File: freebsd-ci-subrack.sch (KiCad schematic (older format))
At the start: 63 parts

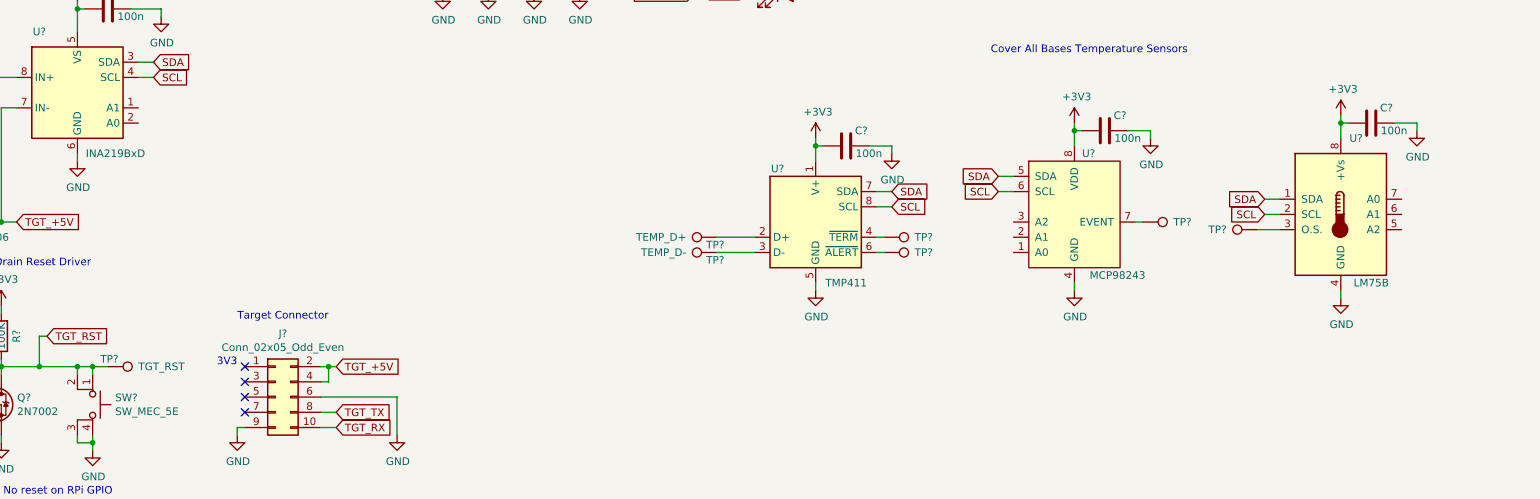
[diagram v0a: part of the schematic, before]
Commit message: I2C address assignment
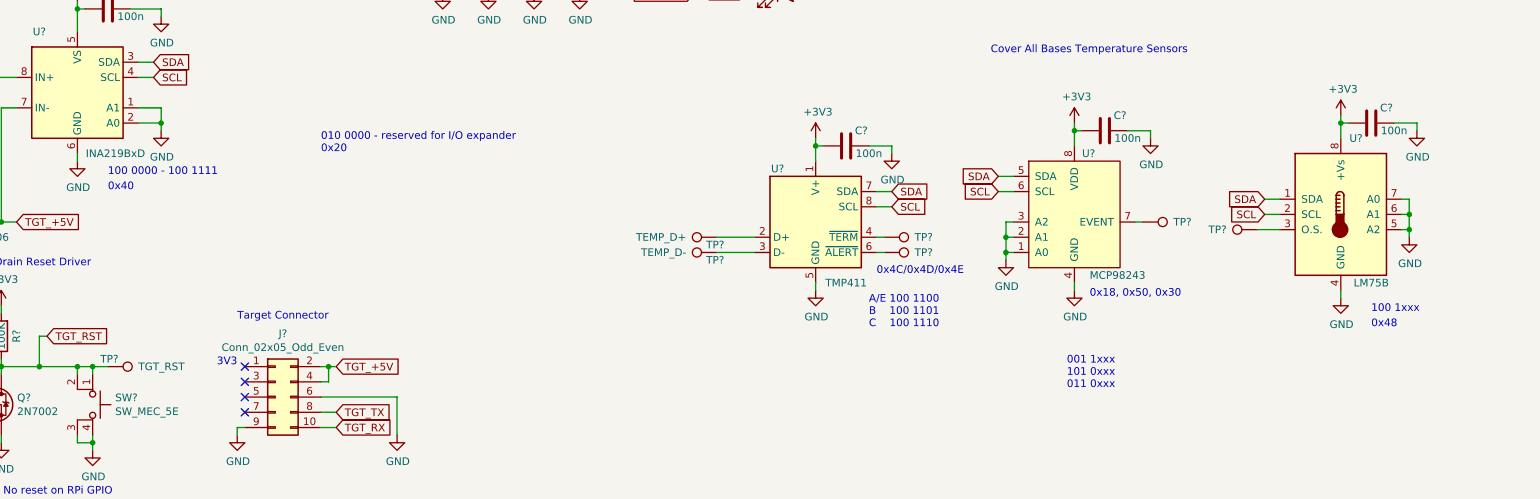
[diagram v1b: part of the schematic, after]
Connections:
- net GND: now also U?.1 (A0), U?.1 (A1), U?.2 (A0), U?.2 (A1), U?.3 (A2), U?.5 (A2), U?.6 (A1), U?.7 (A0)
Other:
- note added: "001 1xxx\n101 0xxx\n011 0xxx"
- note added: "010 0000 - reserved for I/O expander\n0x20"
- note added: "0x18, 0x50, 0x30\n"
- note added: "0x40"
- note added: "0x48"
- note added: "0x4C/0x4D/0x4E"
- note added: "100 0000 - 100 1111\n"
- note added: "100 1xxx"
- note added: "A/E 100 1100\nB 100 1101\nC 100 1110"
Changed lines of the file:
@@
 Text Notes 11800 5750 0    50   ~ 0
 - 98243 for compatibity with L41 design\n- TMP411 for remote sensor\n- LM75B for availability
+Text Notes 8650 6250 0    50   ~ 0
+0x18, 0x50, 0x30\n
+Text Notes 7200 6450 0    50   ~ 0
+A/E 100 1100\nB    100 1101\nC    100 1110
+Text Notes 10500 6350 0    50   ~ 0
+100 1xxx
+$Comp
+L power:GND #PWR?
+U 1 1 60D5940E
+P 8100 6000
+F 0 "#PWR?" H 8100 5750 50  0001 C CNN
+F 1 "GND" H 8105 5827 50  0000 C CNN
+F 2 "" H 8100 6000 50  0001 C CNN
+F 3 "" H 8100 6000 50  0001 C CNN
+	1    8100 6000
+	1    0    0    -1
+$EndComp
+Wire Wire Line
+	8100 6000 8100 5950
+Wire Wire Line
+	8100 5950 8150 5950
+Wire Wire Line
+	8100 5950 8100 5850
+Wire Wire Line
+	8100 5850 8150 5850
+Connection ~ 8100 5950
+Wire Wire Line
+	8100 5850 8100 5750
+Wire Wire Line
+	8100 5750 8150 5750
+Connection ~ 8100 5850
+Text Notes 8500 6850 0    50   ~ 0
+001 1xxx\n101 0xxx\n011 0xxx
+Text Notes 2200 5450 0    50   ~ 0
+100 0000 - 100 1111\n
+Text Notes 10500 6450 0    50   ~ 0
+0x48
+$Comp
+L power:GND #PWR?
+U 1 1 60D90478
+P 10750 5850
+F 0 "#PWR?" H 10750 5600 50  0001 C CNN
+F 1 "GND" H 10755 5677 50  0000 C CNN
+F 2 "" H 10750 5850 50  0001 C CNN
+F 3 "" H 10750 5850 50  0001 C CNN
+	1    10750 5850
+	1    0    0    -1
+$EndComp
+Wire Wire Line
+	10750 5850 10750 5800
+Wire Wire Line
+	10750 5600 10700 5600
+Wire Wire Line
+	10700 5700 10750 5700
+Connection ~ 10750 5700
+Wire Wire Line
+	10750 5700 10750 5600
+Wire Wire Line
+	10700 5800 10750 5800
+Connection ~ 10750 5800
+Wire Wire Line
+	10750 5800 10750 5700
+$Comp
+L power:GND #PWR?
+U 1 1 60DC427E
+P 2550 5150
+F 0 "#PWR?" H 2550 4900 50  0001 C CNN
+F 1 "GND" H 2555 4977 50  0000 C CNN
+F 2 "" H 2550 5150 50  0001 C CNN
+F 3 "" H 2550 5150 50  0001 C CNN
+	1    2550 5150
+	1    0    0    -1
+$EndComp
+Wire Wire Line
+	2400 5100 2550 5100
+Wire Wire Line
+	2550 5100 2550 5150
+Wire Wire Line
+	2400 5000 2550 5000
+Wire Wire Line
+	2550 5000 2550 5100
+Connection ~ 2550 5100
+Text Notes 2200 5550 0    50   ~ 0
+0x40
+Text Notes 7250 6100 0    50   ~ 0
+0x4C/0x4D/0x4E
+Text Notes 3600 5300 0    50   ~ 0
+010 0000 - reserved for I/O expander\n0x20
 $EndSCHEMATC
